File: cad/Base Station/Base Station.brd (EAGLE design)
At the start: 38.1 x 31.8 mm, 4 parts, among them M1 WIRELESS-NRF24L01-PA-EXT

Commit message: Updated board layouts
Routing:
- net CSN: track 23.1 -> 27.5 mm
- net SCK: track 13.5 -> 14.7 mm
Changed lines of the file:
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@@
 <contactref element="C1" pad="2"/>
 <wire x1="33.6042" y1="10.16" x2="33.655" y2="10.16" width="0.254" layer="1"/>
-<wire x1="33.8328" y1="11.303" x2="33.8328" y2="10.16" width="0.254" layer="16"/>
-<wire x1="36.4744" y1="13.9446" x2="33.8328" y2="11.303" width="0.254" layer="16"/>
-<wire x1="36.4744" y1="23.2918" x2="36.4744" y2="13.9446" width="0.254" layer="16"/>
-<wire x1="33.147" y1="26.6192" x2="36.4744" y2="23.2918" width="0.254" layer="16"/>
-<wire x1="33.8328" y1="10.16" x2="33.655" y2="10.16" width="0.254" layer="16"/>
 <wire x1="33.6042" y1="10.16" x2="33.6042" y2="6.9342" width="0.254" layer="1"/>
 <wire x1="33.6042" y1="6.9342" x2="29.21" y2="2.54" width="0.254" layer="1"/>
-<wire x1="33.147" y1="26.6192" x2="33.02" y2="26.67" width="0" layer="19" extent="16-16"/>
-<wire x1="25.4" y1="29.21" x2="33.02" y2="26.67" width="0" layer="19" extent="1-1"/>
+<wire x1="33.02" y1="26.67" x2="36.83" y2="22.86" width="0.254" layer="16"/>
+<wire x1="36.83" y1="22.86" x2="36.83" y2="13.335" width="0.254" layer="16"/>
+<wire x1="36.83" y1="13.335" x2="33.655" y2="10.16" width="0.254" layer="16"/>
 <wire x1="17.78" y1="29.21" x2="25.4" y2="29.21" width="0" layer="19" extent="1-1"/>
 <wire x1="12.7" y1="26.67" x2="17.78" y2="29.21" width="0" layer="19" extent="1-1"/>
 <wire x1="7.62" y1="29.21" x2="12.7" y2="26.67" width="0" layer="19" extent="1-1"/>
+<wire x1="33.02" y1="26.67" x2="25.4" y2="29.21" width="0" layer="19" extent="1-1"/>
 </signal>
 <signal name="3.3V">
@@
 <contactref element="JP1" pad="19"/>
 <contactref element="M1" pad="6"/>
-<wire x1="31.0896" y1="16.1036" x2="31.0896" y2="15.4178" width="0.254" layer="1"/>
-<wire x1="25.6032" y1="21.59" x2="31.0896" y2="16.1036" width="0.254" layer="1"/>
-<wire x1="25.6032" y1="26.6192" x2="25.6032" y2="21.59" width="0.254" layer="1"/>
-<wire x1="31.0896" y1="15.4178" x2="31.115" y2="15.24" width="0.254" layer="1"/>
-<wire x1="25.6032" y1="26.6192" x2="25.4" y2="26.67" width="0" layer="19" extent="1-1"/>
+<wire x1="25.4" y1="26.67" x2="25.4" y2="20.955" width="0.254" layer="16"/>
+<wire x1="25.4" y1="20.955" x2="31.115" y2="15.24" width="0.254" layer="16"/>
 </signal>
 <signal name="SCK">
 <contactref element="JP1" pad="23"/>
 <contactref element="M1" pad="5"/>
-<wire x1="33.8328" y1="16.3322" x2="33.8328" y2="15.4178" width="0.254" layer="16"/>
-<wire x1="34.7472" y1="17.2466" x2="33.8328" y2="16.3322" width="0.254" layer="16"/>
-<wire x1="34.7472" y1="22.5044" x2="34.7472" y2="17.2466" width="0.254" layer="16"/>
-<wire x1="30.6324" y1="26.6192" x2="34.7472" y2="22.5044" width="0.254" layer="16"/>
-<wire x1="33.8328" y1="15.4178" x2="33.655" y2="15.24" width="0.254" layer="16"/>
-<wire x1="30.6324" y1="26.6192" x2="30.48" y2="26.67" width="0" layer="19" extent="16-16"/>
+<wire x1="30.48" y1="26.67" x2="35.56" y2="21.59" width="0.254" layer="16"/>
+<wire x1="35.56" y1="21.59" x2="35.56" y2="16.51" width="0.254" layer="16"/>
+<wire x1="35.56" y1="16.51" x2="34.29" y2="15.24" width="0.254" layer="16"/>
+<wire x1="34.29" y1="15.24" x2="33.655" y2="15.24" width="0.254" layer="16"/>
 </signal>
 <signal name="CSN">
 <contactref element="JP1" pad="24"/>
 <contactref element="M1" pad="4"/>
-<wire x1="31.3182" y1="13.8176" x2="31.3182" y2="12.9032" width="0.254" layer="1"/>
-<wire x1="32.4612" y1="14.9606" x2="31.3182" y2="13.8176" width="0.254" layer="1"/>
-<wire x1="32.4612" y1="24.1046" x2="32.4612" y2="14.9606" width="0.254" layer="1"/>
-<wire x1="34.29" y1="25.9334" x2="32.4612" y2="24.1046" width="0.254" layer="1"/>
-<wire x1="34.29" y1="29.8196" x2="34.29" y2="25.9334" width="0.254" layer="1"/>
-<wire x1="33.6042" y1="30.5054" x2="34.29" y2="29.8196" width="0.254" layer="1"/>
 <wire x1="31.7754" y1="30.5054" x2="33.6042" y2="30.5054" width="0.254" layer="1"/>
-<wire x1="31.3182" y1="12.9032" x2="31.115" y2="12.7" width="0.254" layer="1"/>
 <wire x1="31.7754" y1="30.5054" x2="30.48" y2="29.21" width="0.254" layer="1"/>
+<wire x1="33.6042" y1="30.5054" x2="33.6296" y2="30.48" width="0.254" layer="1"/>
+<wire x1="33.6296" y1="30.48" x2="34.29" y2="30.48" width="0.254" layer="1"/>
+<wire x1="34.29" y1="30.48" x2="35.56" y2="29.21" width="0.254" layer="1"/>
+<wire x1="35.56" y1="29.21" x2="35.56" y2="26.67" width="0.254" layer="1"/>
+<wire x1="35.56" y1="26.67" x2="27.94" y2="19.05" width="0.254" layer="1"/>
+<wire x1="27.94" y1="19.05" x2="27.94" y2="15.24" width="0.254" layer="1"/>
+<wire x1="27.94" y1="15.24" x2="30.48" y2="12.7" width="0.254" layer="1"/>
+<wire x1="30.48" y1="12.7" x2="31.115" y2="12.7" width="0.254" layer="1"/>
 </signal>
 <signal name="CE">
 <contactref element="JP1" pad="15"/>
 <contactref element="M1" pad="3"/>
-<wire x1="29.21" y1="17.78" x2="29.21" y2="15.24" width="0.254" layer="16"/>
-<wire x1="29.21" y1="15.24" x2="30.48" y2="13.97" width="0.254" layer="16"/>
-<wire x1="30.48" y1="13.97" x2="33.02" y2="13.97" width="0.254" layer="16"/>
-<wire x1="33.02" y1="13.97" x2="33.655" y2="13.335" width="0.254" layer="16"/>
-<wire x1="33.655" y1="13.335" x2="33.655" y2="12.7" width="0.254" layer="16"/>
-<wire x1="29.21" y1="17.78" x2="20.32" y2="26.67" width="0.254" layer="16"/>
+<wire x1="20.32" y1="26.67" x2="20.32" y2="24.13" width="0.254" layer="16"/>
+<wire x1="20.32" y1="24.13" x2="30.48" y2="13.97" width="0.254" layer="16"/>
+<wire x1="30.48" y1="13.97" x2="32.385" y2="13.97" width="0.254" layer="16"/>
+<wire x1="32.385" y1="13.97" x2="33.655" y2="12.7" width="0.254" layer="16"/>
 </signal>
 </signals>

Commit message: Updated base station
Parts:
- removed JP1: RASPBERRYPI-GPIOPTH, SparkFun-Boards:2X13-SHROUDED
- removed M1: WIRELESS-NRF24L01-PA-EXT, diy-modules:WIRELESS-NRD24L01-PA-EXT
- added J1: GPIO, pinhead:2X13
- added J2: nRF24L01+, my-custom:FEMALE-2X4-SMT
- added LOGO1: OSHW-LOGOS, SparkFun-Aesthetics:OSHW-LOGO-S
- added U$1: (no value), SparkFun-Aesthetics:OSHW-LOGO-S_COPPER
- C1: device SparkFun-Capacitors:CPOL-RADIAL-10UF-25V -> rcl:C1206K
- FRAME1: value FRAME-LETTER -> FRAME-LETTERNO_PACKAGE; device SparkFun-Aesthetics:CREATIVE_COMMONS -> SparkFun-Aesthetics:DUMMY
- moved FRAME1 120.5 mm to (0.00, 0.00)
- moved C1 8.13 mm to (34.3, 7.62), turned to 0 degrees
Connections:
- removed net 3.3V: JP1.1
- removed net 5V: JP1.2, JP1.4
- net CE: now also J1.15, J2.3; no longer JP1.15, M1.3
- net CSN: now also J1.24, J2.4; no longer JP1.24, M1.4
- net GND: now also J1.14, J1.20, J1.25, J1.6, J1.9, J2.1; no longer JP1.14, JP1.20, JP1.25, JP1.6, JP1.9, M1.1
- net MISO: now also J1.21, J2.7; no longer JP1.21, M1.7
- net MOSI: now also J1.19, J2.6; no longer JP1.19, M1.6
- net SCK: now also J1.23, J2.5; no longer JP1.23, M1.5
- net VCC: now also J1.17, J2.2; no longer JP1.17, M1.2
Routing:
- net GND: track 28.9 -> 0.00 mm
- net CE: track 20.6 -> 30.6 mm
- net MISO: track 11.1 -> 16.2 mm
- net CSN: track 27.5 -> 22.5 mm
- net VCC: track 29.4 -> 24.6 mm
- added copper zone on layer 1, net GND
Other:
- board text added: "ACM@UIUC Base Station V1"
- board text removed: "Alex Cordonnier"

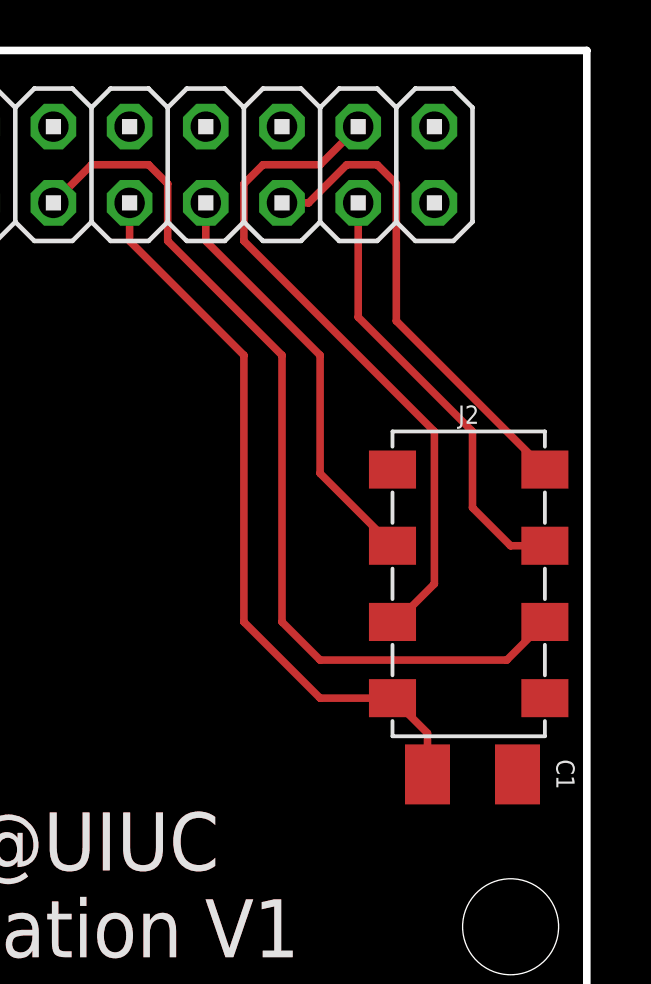
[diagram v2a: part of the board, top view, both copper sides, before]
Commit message: Replaced 2x4 header part
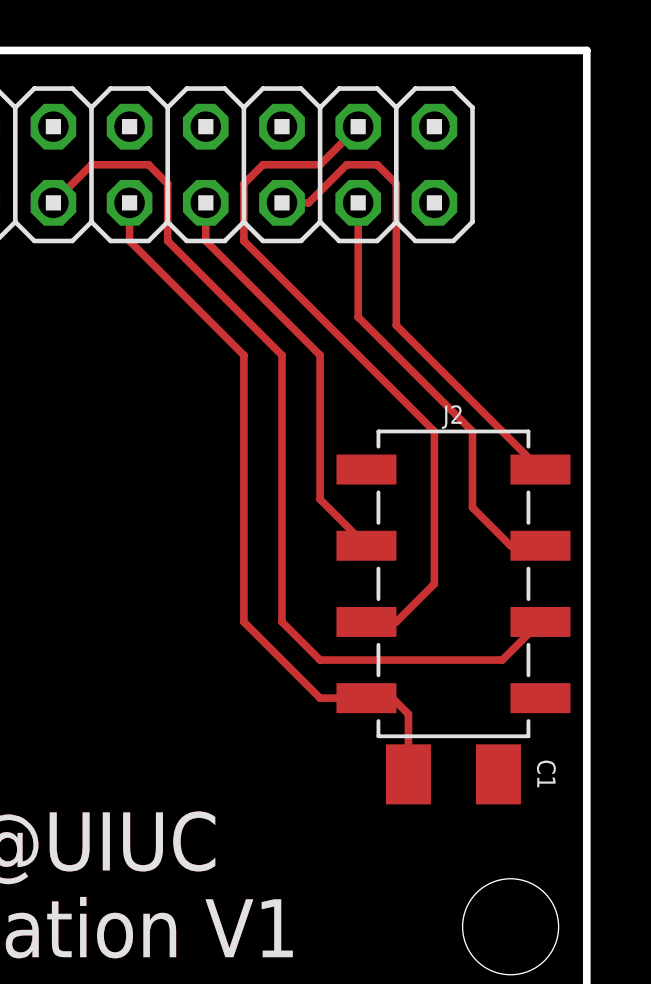
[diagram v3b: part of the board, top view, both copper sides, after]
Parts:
- moved C1 0.63 mm to (33.7, 7.62)
- moved J2 0.51 mm to (33.7, 14.0)
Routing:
- net CSN: track 22.5 -> 23.4 mm
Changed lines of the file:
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@@
 <attribute name="DESIGNER" value="Nobody" x="0" y="0" size="1.778" layer="27" display="off"/>
 </element>
-<element name="C1" library="rcl" package="C1206K" value="10uF" x="34.29" y="7.62" smashed="yes">
-<attribute name="NAME" x="37.084" y="7.62" size="0.6096" layer="25" font="vector" ratio="10" rot="SR270" align="bottom-center"/>
+<element name="C1" library="rcl" package="C1206K" value="10uF" x="33.655" y="7.62" smashed="yes">
+<attribute name="NAME" x="36.449" y="7.62" size="0.6096" layer="25" font="vector" ratio="10" rot="SR270" align="bottom-center"/>
 </element>
-<element name="J2" library="my-custom" package="FEMALE-2X4-SMT" value="nRF24L01+" x="34.163" y="13.97" smashed="yes" rot="R90">
-<attribute name="NAME" x="34.163" y="19.304" size="0.6096" layer="25" font="vector" ratio="10" align="bottom-center"/>
+<element name="J2" library="my-custom" package="FEMALE-2X4-SMT" value="nRF24L01+" x="33.655" y="13.97" smashed="yes" rot="R90">
+<attribute name="NAME" x="33.655" y="19.304" size="0.6096" layer="25" font="vector" ratio="10" align="bottom-center"/>
 </element>
 <element name="LOGO1" library="SparkFun-Aesthetics" package="OSHW-LOGO-S" value="OSHW-LOGOS" x="8.89" y="5.08"/>
@@
 <contactref element="J2" pad="2"/>
 <contactref element="C1" pad="1"/>
-<wire x1="29.21" y1="10.16" x2="31.623" y2="10.16" width="0.254" layer="1"/>
+<wire x1="29.21" y1="10.16" x2="30.755" y2="10.16" width="0.254" layer="1"/>
 <wire x1="22.86" y1="26.67" x2="22.86" y2="25.4" width="0.254" layer="1"/>
 <wire x1="22.86" y1="25.4" x2="26.67" y2="21.59" width="0.254" layer="1"/>
@@
 <wire x1="26.67" y1="12.7" x2="29.21" y2="10.16" width="0.254" layer="1"/>
 <contactref element="J1" pad="17"/>
-<wire x1="31.623" y1="10.16" x2="32.79" y2="8.993" width="0.254" layer="1"/>
-<wire x1="32.79" y1="8.993" x2="32.79" y2="7.62" width="0.254" layer="1"/>
+<wire x1="30.755" y1="10.16" x2="31.623" y2="10.16" width="0.254" layer="1"/>
+<wire x1="31.623" y1="10.16" x2="32.155" y2="9.628" width="0.254" layer="1"/>
+<wire x1="32.155" y1="9.628" x2="32.155" y2="7.62" width="0.254" layer="1"/>
 </signal>
 <signal name="MISO">
@@
 <wire x1="30.099" y1="27.94" x2="31.115" y2="27.94" width="0.254" layer="1"/>
 <wire x1="31.115" y1="27.94" x2="31.75" y2="27.305" width="0.254" layer="1"/>
-<wire x1="31.75" y1="27.305" x2="31.75" y2="22.733" width="0.254" layer="1"/>
-<wire x1="31.75" y1="22.733" x2="36.703" y2="17.78" width="0.254" layer="1"/>
+<wire x1="31.75" y1="27.305" x2="31.75" y2="22.585" width="0.254" layer="1"/>
+<wire x1="31.75" y1="22.585" x2="36.555" y2="17.78" width="0.254" layer="1"/>
 </signal>
 <signal name="MOSI">
@@
 <wire x1="25.4" y1="25.4" x2="29.21" y2="21.59" width="0.254" layer="1"/>
 <contactref element="J1" pad="19"/>
-<wire x1="29.21" y1="21.59" x2="29.21" y2="17.653" width="0.254" layer="1"/>
-<wire x1="29.21" y1="17.653" x2="31.623" y2="15.24" width="0.254" layer="1"/>
+<wire x1="29.21" y1="21.59" x2="29.21" y2="16.785" width="0.254" layer="1"/>
+<wire x1="29.21" y1="16.785" x2="30.755" y2="15.24" width="0.254" layer="1"/>
 </signal>
 <signal name="SCK">
@@
 <wire x1="30.48" y1="22.86" x2="34.29" y2="19.05" width="0.254" layer="1"/>
 <wire x1="34.29" y1="19.05" x2="34.29" y2="16.51" width="0.254" layer="1"/>
-<wire x1="34.29" y1="16.51" x2="35.56" y2="15.24" width="0.254" layer="1"/>
-<wire x1="35.56" y1="15.24" x2="36.703" y2="15.24" width="0.254" layer="1"/>
+<wire x1="36.555" y1="15.24" x2="35.56" y2="15.24" width="0.254" layer="1"/>
+<wire x1="35.56" y1="15.24" x2="34.29" y2="16.51" width="0.254" layer="1"/>
 </signal>
 <signal name="CSN">
@@
 <contactref element="J1" pad="24"/>
 <wire x1="33.02" y1="19.05" x2="33.02" y2="13.97" width="0.254" layer="1"/>
-<wire x1="33.02" y1="13.97" x2="31.75" y2="12.7" width="0.254" layer="1"/>
-<wire x1="31.75" y1="12.7" x2="31.623" y2="12.7" width="0.254" layer="1"/>
+<wire x1="30.755" y1="12.7" x2="31.75" y2="12.7" width="0.254" layer="1"/>
+<wire x1="31.75" y1="12.7" x2="33.02" y2="13.97" width="0.254" layer="1"/>
 </signal>
 <signal name="CE">
@@
 <wire x1="21.59" y1="27.94" x2="23.495" y2="27.94" width="0.254" layer="1"/>
 <wire x1="23.495" y1="27.94" x2="24.13" y2="27.305" width="0.254" layer="1"/>
-<wire x1="29.21" y1="11.43" x2="35.433" y2="11.43" width="0.254" layer="1"/>
 <wire x1="24.13" y1="27.305" x2="24.13" y2="25.4" width="0.254" layer="1"/>
 <wire x1="24.13" y1="25.4" x2="27.94" y2="21.59" width="0.254" layer="1"/>
@@
 <wire x1="27.94" y1="12.7" x2="29.21" y2="11.43" width="0.254" layer="1"/>
 <contactref element="J1" pad="15"/>
-<wire x1="35.433" y1="11.43" x2="36.703" y2="12.7" width="0.254" layer="1"/>
+<wire x1="29.21" y1="11.43" x2="35.285" y2="11.43" width="0.254" layer="1"/>
+<wire x1="35.285" y1="11.43" x2="36.555" y2="12.7" width="0.254" layer="1"/>
 </signal>
 </signals>

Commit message: Minor adjustments
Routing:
- net MISO: track 16.1 -> 16.7 mm
- net MOSI: track 13.6 -> 14.2 mm
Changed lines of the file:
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@@
 <wire x1="30.099" y1="27.94" x2="31.115" y2="27.94" width="0.254" layer="1"/>
 <wire x1="31.115" y1="27.94" x2="31.75" y2="27.305" width="0.254" layer="1"/>
-<wire x1="31.75" y1="27.305" x2="31.75" y2="22.585" width="0.254" layer="1"/>
-<wire x1="31.75" y1="22.585" x2="36.555" y2="17.78" width="0.254" layer="1"/>
+<wire x1="31.75" y1="27.305" x2="31.75" y2="22.86" width="0.254" layer="1"/>
+<wire x1="31.75" y1="22.86" x2="34.925" y2="19.685" width="0.254" layer="1"/>
+<wire x1="34.925" y1="19.685" x2="34.925" y2="18.415" width="0.254" layer="1"/>
+<wire x1="34.925" y1="18.415" x2="35.56" y2="17.78" width="0.254" layer="1"/>
+<wire x1="35.56" y1="17.78" x2="36.555" y2="17.78" width="0.254" layer="1"/>
 </signal>
 <signal name="MOSI">
 <contactref element="J2" pad="6"/>
 <wire x1="25.4" y1="26.67" x2="25.4" y2="25.4" width="0.254" layer="1"/>
+<contactref element="J1" pad="19"/>
 <wire x1="25.4" y1="25.4" x2="29.21" y2="21.59" width="0.254" layer="1"/>
-<contactref element="J1" pad="19"/>
-<wire x1="29.21" y1="21.59" x2="29.21" y2="16.785" width="0.254" layer="1"/>
-<wire x1="29.21" y1="16.785" x2="30.755" y2="15.24" width="0.254" layer="1"/>
+<wire x1="29.21" y1="21.59" x2="29.21" y2="15.875" width="0.254" layer="1"/>
+<wire x1="29.21" y1="15.875" x2="29.845" y2="15.24" width="0.254" layer="1"/>
+<wire x1="29.845" y1="15.24" x2="30.755" y2="15.24" width="0.254" layer="1"/>
 </signal>
 <signal name="SCK">
@@
 <wire x1="27.94" y1="12.7" x2="29.21" y2="11.43" width="0.254" layer="1"/>
 <contactref element="J1" pad="15"/>
-<wire x1="29.21" y1="11.43" x2="35.285" y2="11.43" width="0.254" layer="1"/>
-<wire x1="35.285" y1="11.43" x2="36.555" y2="12.7" width="0.254" layer="1"/>
+<wire x1="29.21" y1="11.43" x2="33.02" y2="11.43" width="0.254" layer="1"/>
+<wire x1="33.02" y1="11.43" x2="34.29" y2="12.7" width="0.254" layer="1"/>
+<wire x1="34.29" y1="12.7" x2="36.555" y2="12.7" width="0.254" layer="1"/>
 </signal>
 </signals>
